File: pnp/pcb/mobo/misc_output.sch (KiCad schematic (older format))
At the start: 39 parts, among them J10 MF3, J11 MF4, J12 DOWNWARDS_LIGHT, J13 UPWARDS_LIGHT, J14 5V_INJECTION, J16 RS-485_2, J17 RS-485_3, J21 AUX1, J22 AUX2, J23 QWIIC1, J24 QWIIC2, J25 RS-485_1, J6 SERVO1, J7 SERVO2, J8 MF1, J9 MF2, Q1 IRF540N, Q2 IRF540N, Q3 IRF540N, Q4 IRF540N, U2 SP3485EN, U3 SP3485EN, U4 SP3485EN

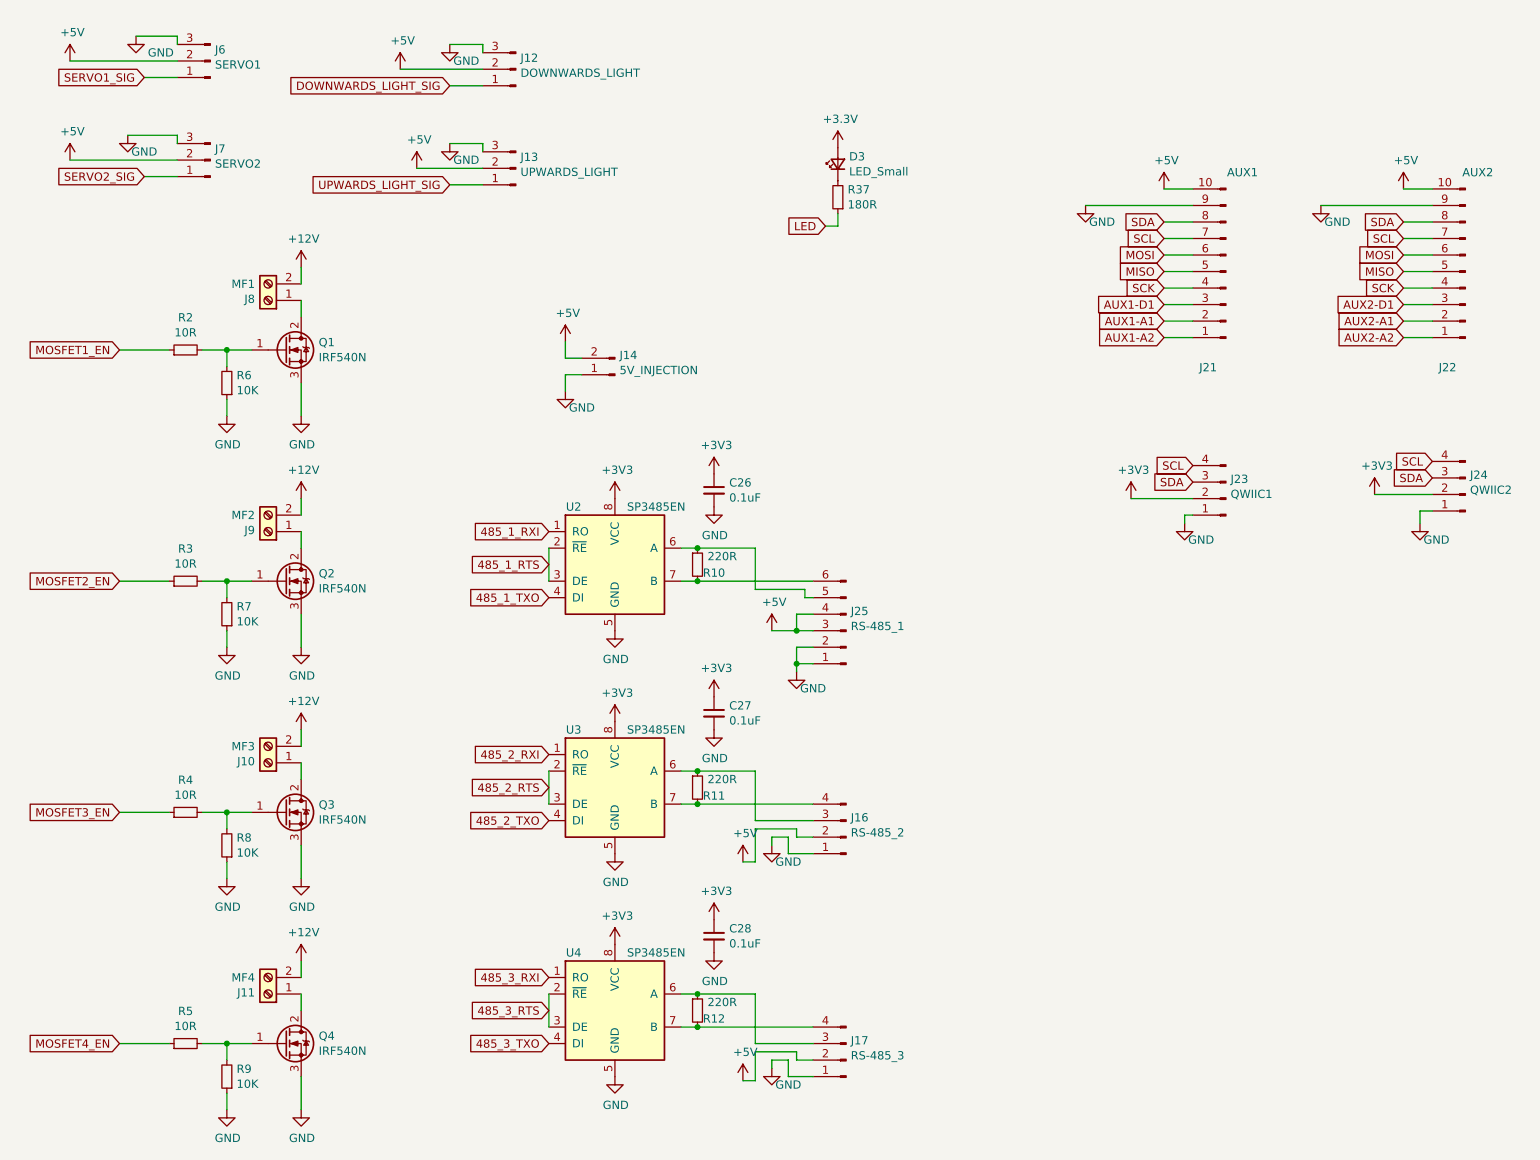
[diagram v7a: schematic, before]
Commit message: Add MOSFET driver and freewheeling diodes
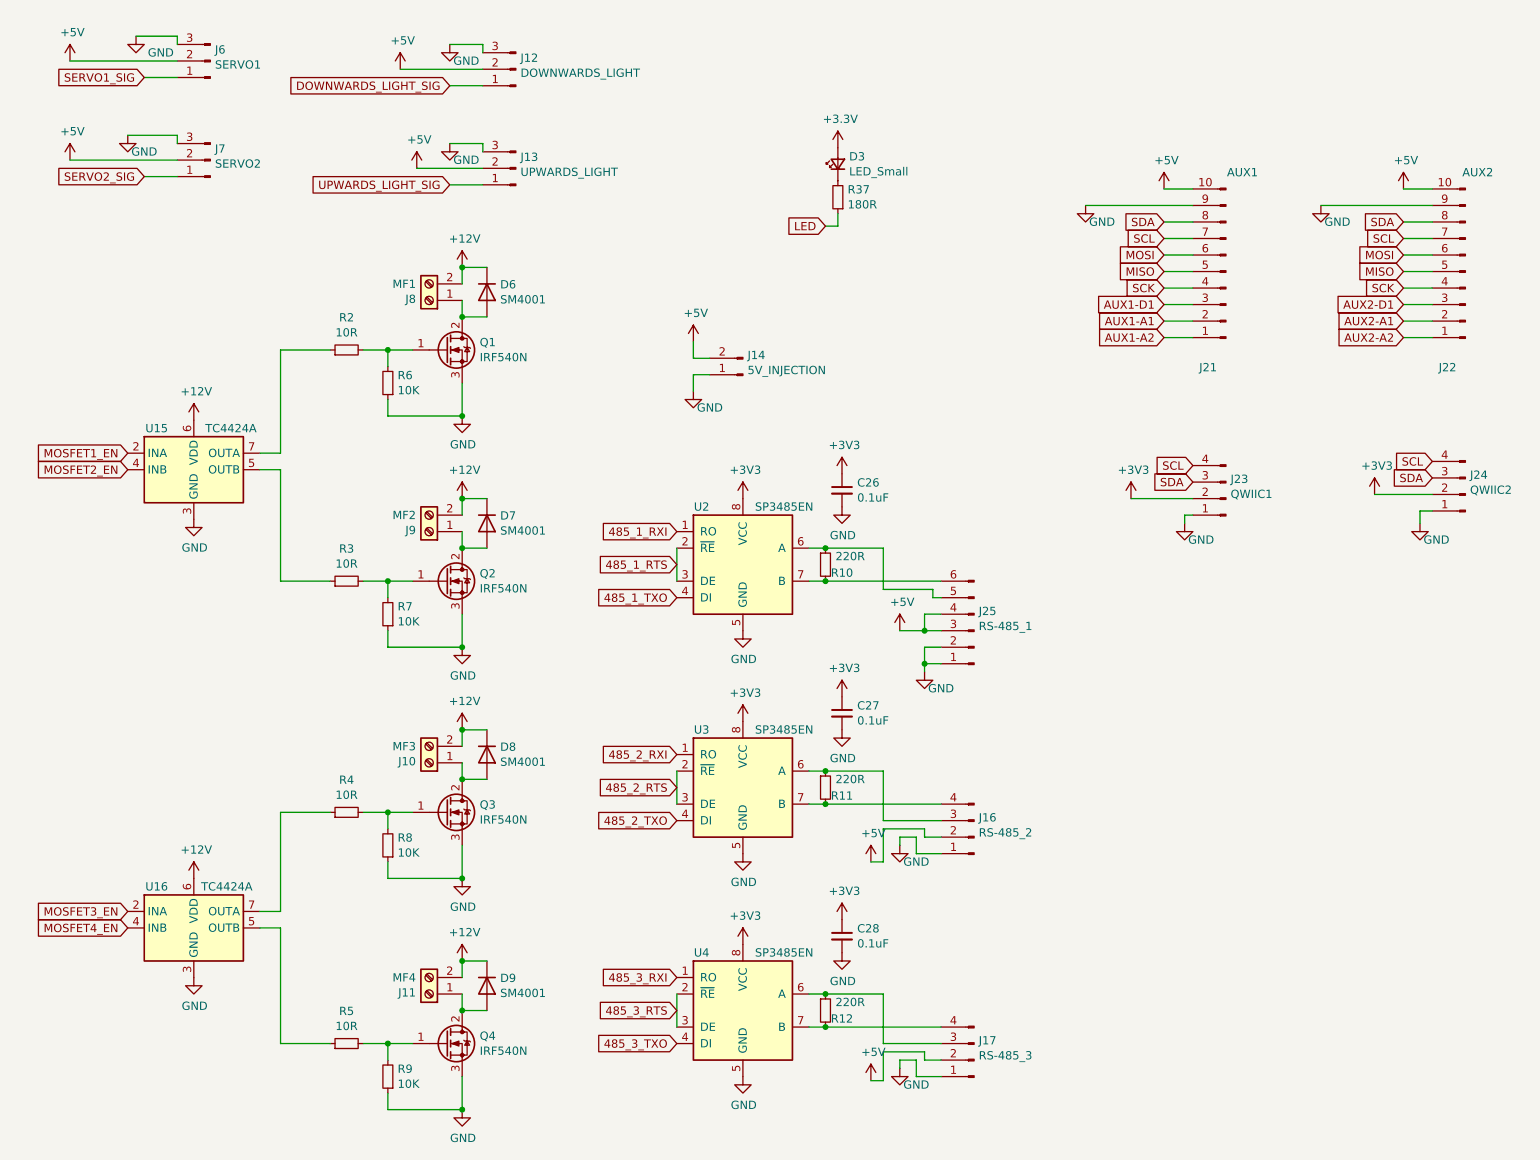
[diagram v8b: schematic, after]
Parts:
- added D6, D7, D8, D9: SM4001, Diode_SMD:D_SOD-123F, symbol Diode:SM4001
- added U15, U16: TC4424A, Package_SO:SOIC-8_3.9x4.9mm_P1.27mm, symbol index:TC4424A
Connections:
- net +12V: now also D6.1 (K), D7.1 (K), D8.1 (K), D9.1 (K), U15.6 (VDD), U16.6 (VDD)
- net GND: now also U15.3 (GND), U16.3 (GND)
- net MOSFET1_EN: now also U15.2 (INA); no longer R2.1
- net MOSFET2_EN: now also U15.4 (INB); no longer R3.1
- net MOSFET3_EN: now also U16.2 (INA); no longer R4.1
- net MOSFET4_EN: now also U16.4 (INB); no longer R5.1
- net at J8.1 (Pin_1), Q1.2 (D): now also D6.2 (A)
- net at J9.1 (Pin_1), Q2.2 (D): now also D7.2 (A)
- net at J10.1 (Pin_1), Q3.2 (D): now also D8.2 (A)
- net at J11.1 (Pin_1), Q4.2 (D): now also D9.2 (A)
- new net: R2.1, U15.7 (OUTA)
- new net: R3.1, U15.5 (OUTB)
- new net: R4.1, U16.7 (OUTA)
- new net: R5.1, U16.5 (OUTB)
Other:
- moved on the sheet: C26, C27, C28, J10, J11, J14, J16, J17, J25, J8, J9, Q1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
